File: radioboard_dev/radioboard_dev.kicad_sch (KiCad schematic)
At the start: 2 parts

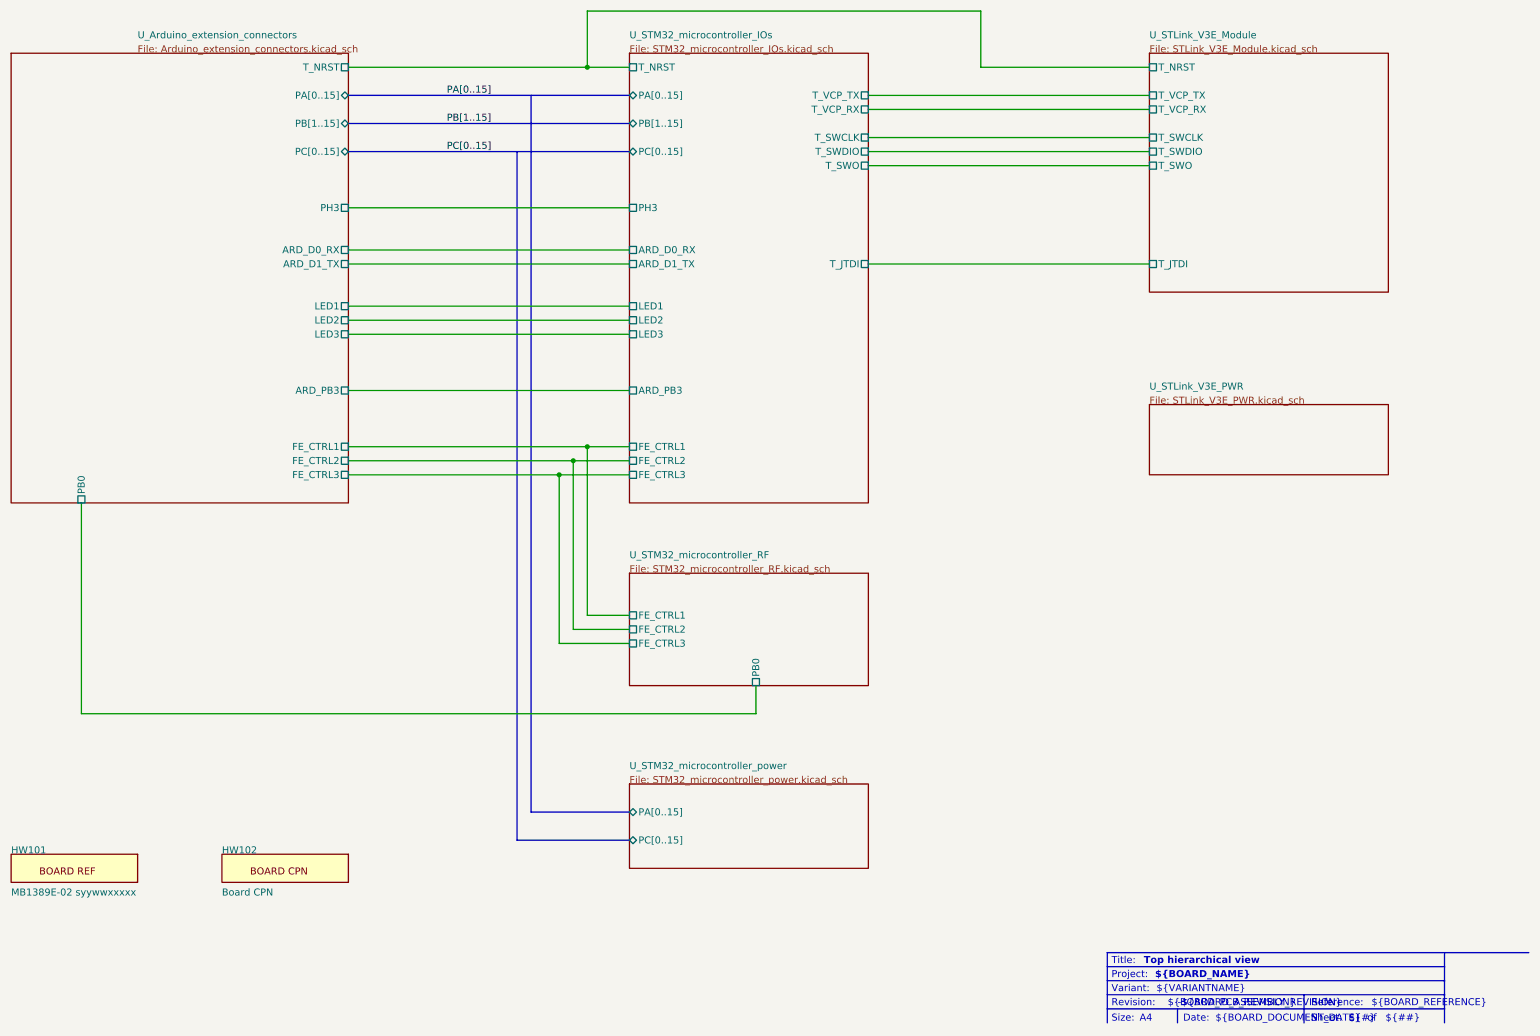
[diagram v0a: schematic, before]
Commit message: added components
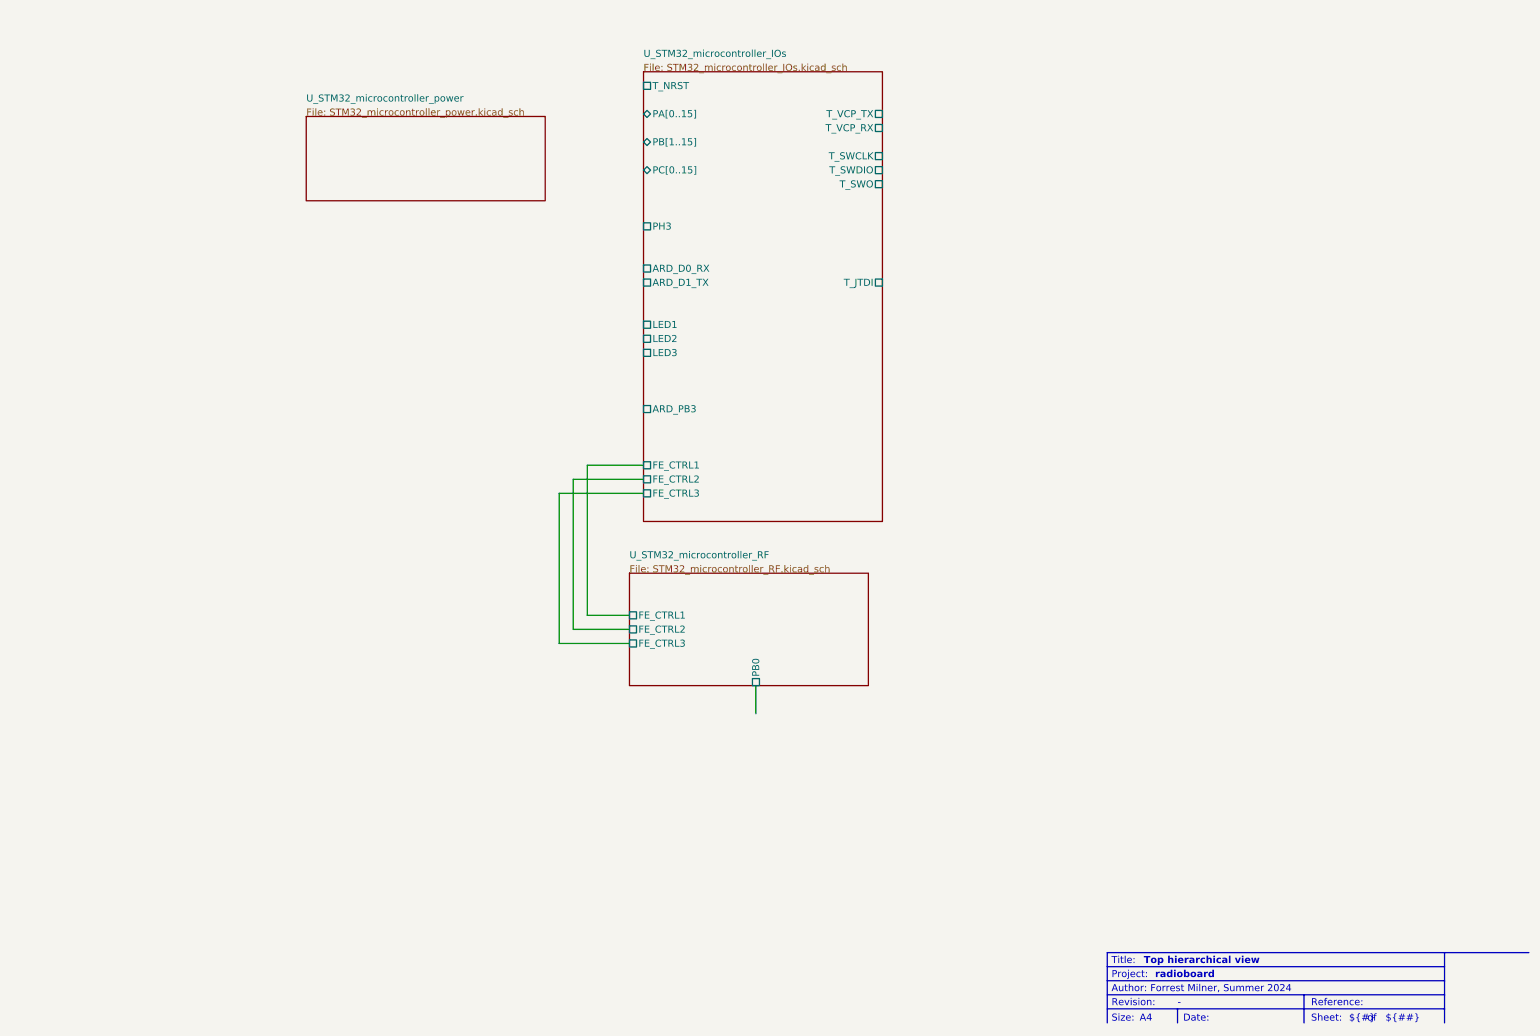
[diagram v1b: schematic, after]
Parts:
- removed HW101: (no value), STICKER_BOARD-REF_25X5, symbol MB1389-altium-import:root_0_STICKER_BOARD_REF
- removed HW102: (no value), STICKER_BOARD-CPN_25X5, symbol MB1389-altium-import:root_0_STICKER_BOARD_CPN
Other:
- removed sheet U_Arduino_extension_connectors
- removed sheet U_STLink_V3E_Module
- removed sheet U_STLink_V3E_PWR
- sheet U_STM32_microcontroller_power ports: added none; removed PA[0..15], PC[0..15]
- note added: "Author: Forrest Milner, Summer 2024"
- note added: "radioboard"
- note removed: "${BOARD_ASSEMBLY_REVISION}"
- note removed: "${BOARD_DOCUMENT_DATE}"
- note removed: "${BOARD_NAME}"
- note removed: "${BOARD_PCB_REVISION}"
- note removed: "${BOARD_REFERENCE}"
- note removed: "${VARIANTNAME}"
- note removed: "Variant:"

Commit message: finish schematic and clear pcb
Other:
- sheet U_STM32_microcontroller_IOs ports: added none; removed ARD_D0_RX, ARD_D1_TX, ARD_PB3, LED1, LED2, LED3, PA[0..15], PB[1..15], PC[0..15], PH3, T_JTDI, T_NRST, T_SWCLK, T_SWDIO, T_SWO, T_VCP_RX, T_VCP_TX
- sheet U_STM32_microcontroller_RF ports: added none; removed PB0

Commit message: added gps
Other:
- sheet U_STM32_microcontroller_IOs renamed microcontroller_IOs
- sheet U_STM32_microcontroller_RF renamed microcontroller_RF
- sheet U_STM32_microcontroller_power renamed microcontroller_power
- added sheet GPS (radioboard_GPS.kicad_sch)
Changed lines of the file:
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@@
 			(color 128 255 128 1.0000)
 		)
-		(property "Sheetname" "U_STM32_microcontroller_power"
-			(at 71.12 43.18 0)
+		(property "Sheetname" "microcontroller_power"
+			(at 71.12 45.0084 0)
 			(effects
 				(font
@@
 		)
 		(property "Sheetfile" "STM32_microcontroller_power.kicad_sch"
-			(at 71.12 45.72 0)
+			(at 71.12 61.5446 0)
+			(effects
+				(font
+					(size 1.27 1.27)
+				)
+				(justify left top)
+			)
+		)
+		(instances
+			(project "radioboard_dev"
+				(path "/d463a497-8f2e-444e-8cd9-7512b15bd4f7"
+					(page "3")
+				)
+			)
+		)
+	)
+	(sheet
+		(at 67.945 78.105)
+		(size 44.45 19.05)
+		(fields_autoplaced yes)
+		(stroke
+			(width 0.1524)
+			(type solid)
+		)
+		(fill
+			(color 0 0 0 0.0000)
+		)
+		(property "Sheetname" "GPS"
+			(at 67.945 77.3934 0)
 			(effects
 				(font
@@
 			)
 		)
+		(property "Sheetfile" "radioboard_GPS.kicad_sch"
+			(at 67.945 97.7396 0)
+			(effects
+				(font
+					(size 1.27 1.27)
+				)
+				(justify left top)
+			)
+		)
 		(instances
 			(project "radioboard_dev"
 				(path "/d463a497-8f2e-444e-8cd9-7512b15bd4f7"
-					(page "3")
+					(page "5")
 				)
 			)
@@
 			(color 128 255 128 1.0000)
 		)
-		(property "Sheetname" "U_STM32_microcontroller_RF"
-			(at 129.54 125.73 0)
+		(property "Sheetname" "microcontroller_RF"
+			(at 129.54 127.5584 0)
 			(effects
 				(font
@@
 		)
 		(property "Sheetfile" "STM32_microcontroller_RF.kicad_sch"
-			(at 129.54 128.27 0)
+			(at 129.54 149.1746 0)
 			(effects
 				(font
 					(size 1.27 1.27)
 				)
-				(justify left bottom)
+				(justify left top)
 			)
 		)
@@
 			(color 128 255 128 1.0000)
 		)
-		(property "Sheetname" "U_STM32_microcontroller_IOs"
-			(at 132.08 35.56 0)
+		(property "Sheetname" "microcontroller_IOs"
+			(at 132.08 37.3884 0)
 			(effects
 				(font
@@
 		)
 		(property "Sheetfile" "STM32_microcontroller_IOs.kicad_sch"
-			(at 132.08 38.1 0)
+			(at 132.08 119.9646 0)
 			(effects
 				(font
 					(size 1.27 1.27)
 				)
-				(justify left bottom)
+				(justify left top)
 			)
 		)
